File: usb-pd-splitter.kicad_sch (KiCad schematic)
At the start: 5 parts, among them J1 USB_C_Receptacle_USB2.0_14P, J2 USB_C_Receptacle_USB2.0_14P, J3 USB_C_Receptacle_USB2.0_14P

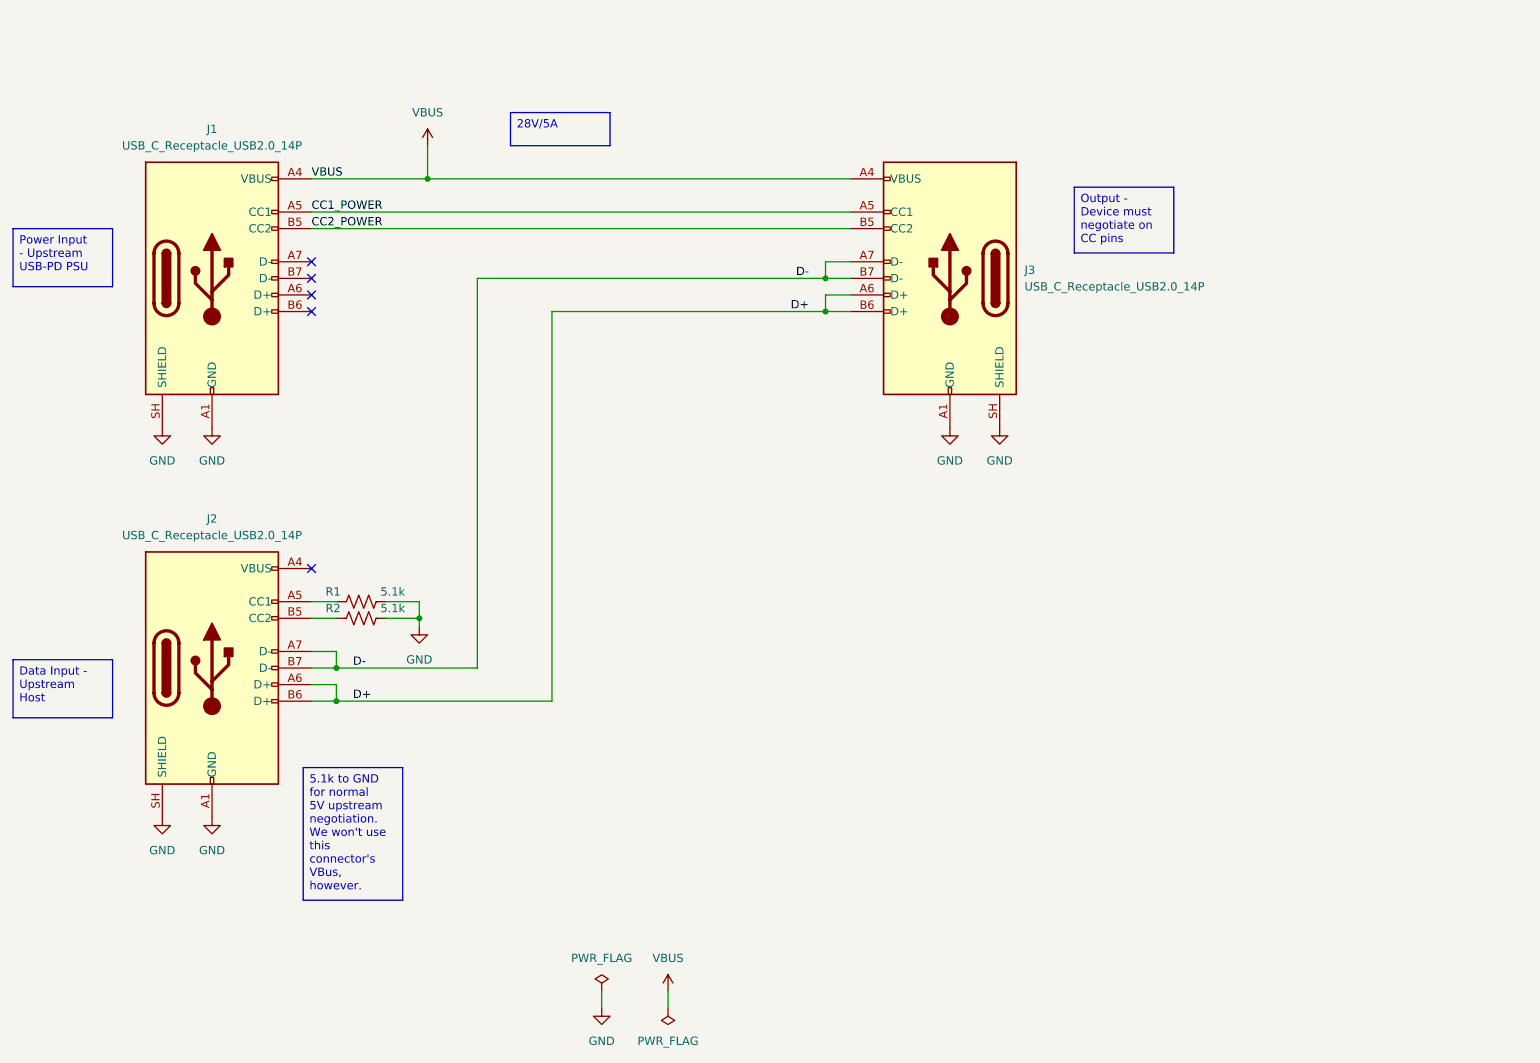
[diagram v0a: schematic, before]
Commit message: routing complete, drc pass
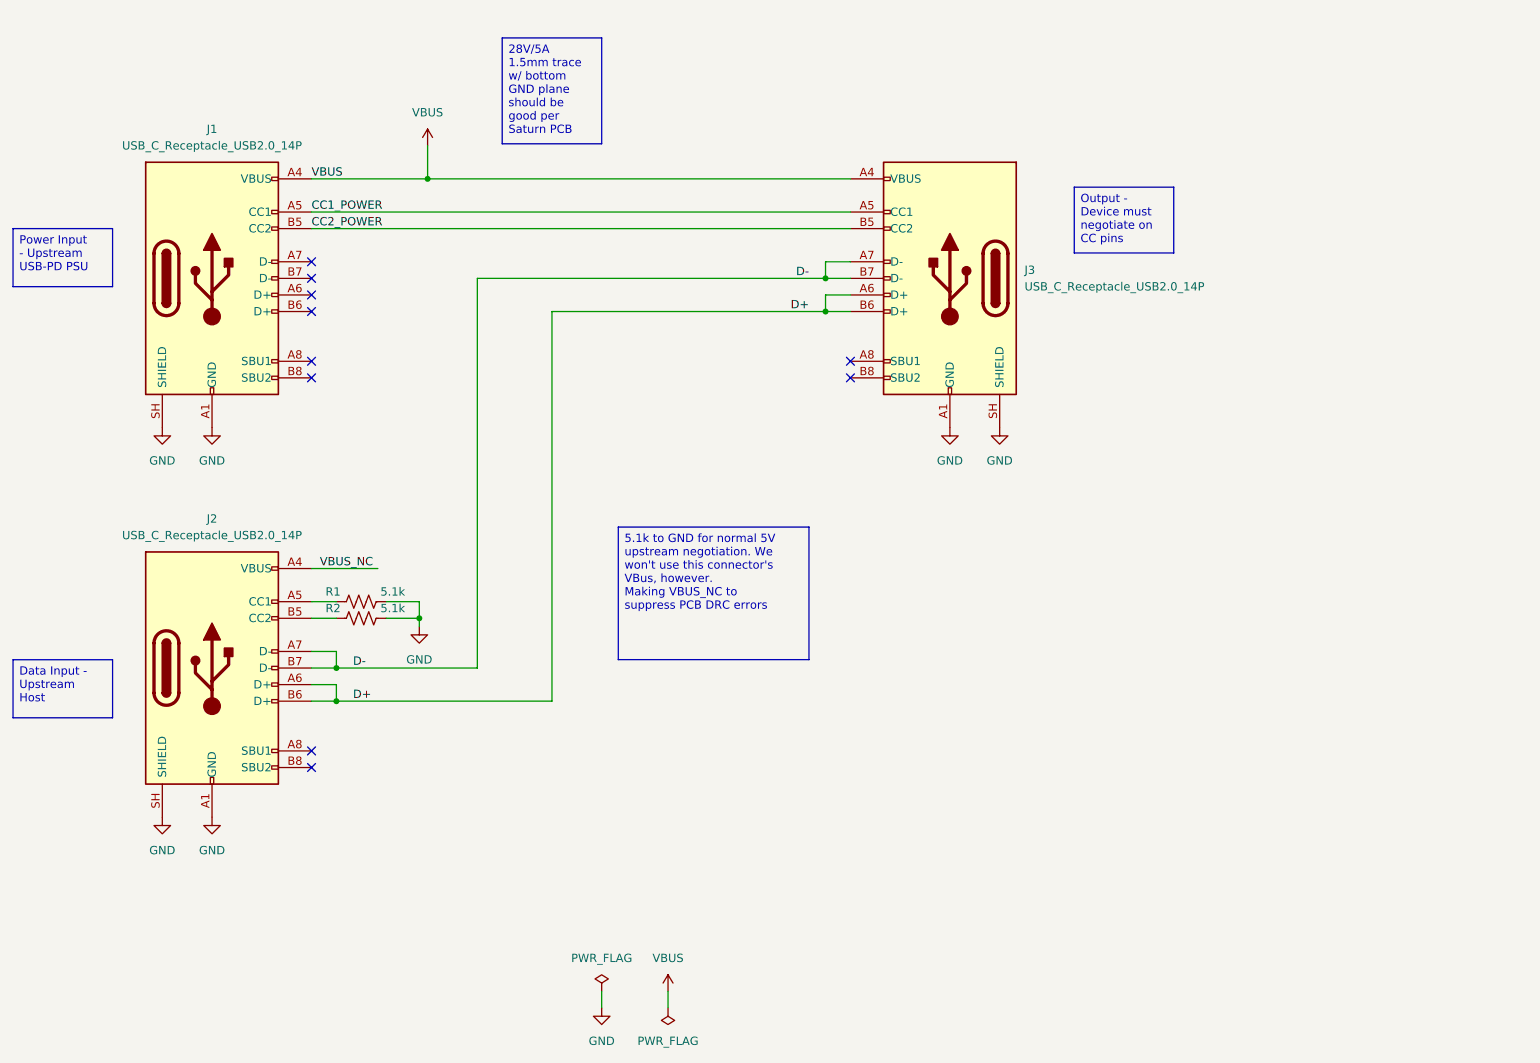
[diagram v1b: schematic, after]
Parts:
- J1, J2, J3: symbol Connector:USB_C_Receptacle_USB2.0_14P -> Connector:USB_C_Receptacle_USB2.0_16P
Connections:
- net VBUS_NC: now reaches J2.A4 (VBUS), J2.A9 (VBUS), J2.B4 (VBUS), J2.B9 (VBUS)
- no-connect marks 5 -> 10
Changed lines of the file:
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@@
 		)
 	)
-	(text_box "28V/5A\n"
+	(text_box "28V/5A\n1.5mm trace w/ bottom GND plane should be good per Saturn PCB"
 		(exclude_from_sim no)
-		(at 107.95 45.72 0)
-		(size 15.24 5.08)
+		(at 106.68 34.29 0)
+		(size 15.24 16.2161)
 		(margins 0.9525 0.9525 0.9525 0.9525)
 		(stroke
@@
 		)
 	)
-	(text_box "5.1k to GND for normal 5V upstream negotiation. We won't use this connector's VBus, however.\n"
+	(text_box "5.1k to GND for normal 5V upstream negotiation. We won't use this connector's VBus, however.\nMaking VBUS_NC to suppress PCB DRC errors\n"
 		(exclude_from_sim no)
-		(at 76.2 146.0647 0)
-		(size 15.24 20.3053)
+		(at 124.46 109.22 0)
+		(size 29.21 20.3053)
 		(margins 0.9525 0.9525 0.9525 0.9525)
 		(stroke
@@
 	)
 	(no_connect
+		(at 160.02 86.36)
+	)
+	(no_connect
+		(at 77.47 86.36)
+	)
+	(no_connect
+		(at 77.47 143.51)
+	)
+	(no_connect
+		(at 77.47 83.82)
+	)
+	(no_connect
+		(at 160.02 83.82)
+	)
+	(no_connect
+		(at 77.47 146.05)
+	)
+	(no_connect
 		(at 77.47 73.66)
 	)
@@
 		(at 77.47 76.2)
 	)
-	(no_connect
-		(at 77.47 115.57)
-	)
 	(wire
 		(pts
@@
 		(pts
 			(xy 160.02 71.12) (xy 156.21 71.12)
+		)
+		(stroke
+			(width 0)
+			(type default)
+		)
+	)
+	(wire
+		(pts
+			(xy 77.47 115.57) (xy 87.63 115.57)
 		)
 		(stroke
@@
 	(label "VBUS"
 		(at 77.47 55.88 0)
+		(effects
+			(font
+				(size 1.27 1.27)
+			)
+			(justify left bottom)
+		)
+	)
+	(label "VBUS_NC"
+		(at 78.74 115.57 0)
 		(effects
 			(font
@@
 	)
 	(symbol
-		(lib_id "Connector:USB_C_Receptacle_USB2.0_14P")
+		(lib_id "Connector:USB_C_Receptacle_USB2.0_16P")
 		(at 62.23 130.81 0)
 		(unit 1)
@@
 		)
 		(pin "B1"
+		)
+		(pin "B8"
+		)
+		(pin "A8"
 		)
 		(instances
@@
 	)
 	(symbol
-		(lib_id "Connector:USB_C_Receptacle_USB2.0_14P")
+		(lib_id "Connector:USB_C_Receptacle_USB2.0_16P")
 		(at 175.26 71.12 0)
 		(mirror y)
@@
 		)
 		(pin "A9"
+		)
+		(pin "B8"
+		)
+		(pin "A8"
 		)
 		(instances
@@
 	)
 	(symbol
-		(lib_id "Connector:USB_C_Receptacle_USB2.0_14P")
+		(lib_id "Connector:USB_C_Receptacle_USB2.0_16P")
 		(at 62.23 71.12 0)
 		(unit 1)
@@
 		(pin "B7"
 		)
+		(pin "A8"
+		)
+		(pin "B8"
+		)
 		(instances

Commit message: Add deterministic hardware release workflow and README 3D render
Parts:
- J1, J2, J3: BOM Comments (none) -> JLCPCB extended part; high assembly difficulty; fixture req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; LCSC Part # (none) -> C5143397; MPN (none) -> USB4110-GF-A; Manufacturer (none) -> Global Connector Technology
- R1, R2: BOM Comments (none) -> JLCPCB basic part; 5.1 kOhm 1% 125 mW; LCSC Part # (none) -> C27834; MPN (none) -> 0805W8F5101T5E; Manufacturer (none) -> UNI-ROYAL
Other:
- title: (none) -> USB-PD Splitter
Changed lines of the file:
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@@
 	(generator_version "10.0")
 	(paper "A4")
+	(title_block
+		(title "USB-PD Splitter")
+		(date "2026-07-18")
+		(rev "A")
+		(comment 1 "Professional fabrication and assembly release")
+		(comment 2 "Hardware version 1.0.0")
+	)
 	(text_box "Output - Device must negotiate on CC pins"
 		(exclude_from_sim no)
@@
 	(wire
 		(pts
-			(xy 77.47 115.57) (xy 87.63 115.57)
+			(xy 77.47 115.57) (xy 78.74 115.57)
 		)
 		(stroke
@@
 			)
 		)
-		(property "Datasheet" "https://www.usb.org/sites/default/files/documents/usb_type-c.zip"
+		(property "Datasheet" "https://gct.co/files/drawings/usb4110.pdf"
 			(at 66.04 130.81 0)
 			(hide yes)
@@
 			)
 		)
+		(property "Manufacturer" "Global Connector Technology" (at 62.23 130.81 0) (hide yes) (effects (font (size 1.27 1.27))))
+		(property "MPN" "USB4110-GF-A" (at 62.23 130.81 0) (hide yes) (effects (font (size 1.27 1.27))))
+		(property "LCSC Part #" "C5143397" (at 62.23 130.81 0) (hide yes) (effects (font (size 1.27 1.27))))
+		(property "BOM Comments" "JLCPCB extended part; high assembly difficulty; fixture required" (at 62.23 130.81 0) (hide yes) (effects (font (size 1.27 1.27))))
 		(pin "A4"
 		)
@@
 			)
 		)
-		(property "Datasheet" ""
+		(property "Datasheet" "https://www.lcsc.com/product-detail/C27834.html"
 			(at 85.09 120.65 0)
 			(hide yes)
@@
 			)
 		)
+		(property "Manufacturer" "UNI-ROYAL" (at 85.09 120.65 0) (hide yes) (effects (font (size 1.27 1.27))))
+		(property "MPN" "0805W8F5101T5E" (at 85.09 120.65 0) (hide yes) (effects (font (size 1.27 1.27))))
+		(property "LCSC Part #" "C27834" (at 85.09 120.65 0) (hide yes) (effects (font (size 1.27 1.27))))
+		(property "BOM Comments" "JLCPCB basic part; 5.1 kOhm 1% 125 mW" (at 85.09 120.65 0) (hide yes) (effects (font (size 1.27 1.27))))
 		(pin "2"
 		)
@@
 			)
 		)
-		(property "Datasheet" "https://www.usb.org/sites/default/files/documents/usb_type-c.zip"
+		(property "Datasheet" "https://gct.co/files/drawings/usb4110.pdf"
 			(at 171.45 71.12 0)
 			(hide yes)
@@
 			)
 		)
+		(property "Manufacturer" "Global Connector Technology" (at 175.26 71.12 0) (hide yes) (effects (font (size 1.27 1.27))))
+		(property "MPN" "USB4110-GF-A" (at 175.26 71.12 0) (hide yes) (effects (font (size 1.27 1.27))))
+		(property "LCSC Part #" "C5143397" (at 175.26 71.12 0) (hide yes) (effects (font (size 1.27 1.27))))
+		(property "BOM Comments" "JLCPCB extended part; high assembly difficulty; fixture required" (at 175.26 71.12 0) (hide yes) (effects (font (size 1.27 1.27))))
 		(pin "B5"
 		)
@@
 			)
 		)
-		(property "Datasheet" ""
+		(property "Datasheet" "https://www.lcsc.com/product-detail/C27834.html"
 			(at 85.09 123.19 0)
 			(hide yes)
@@
 			)
 		)
+		(property "Manufacturer" "UNI-ROYAL" (at 85.09 123.19 0) (hide yes) (effects (font (size 1.27 1.27))))
+		(property "MPN" "0805W8F5101T5E" (at 85.09 123.19 0) (hide yes) (effects (font (size 1.27 1.27))))
+		(property "LCSC Part #" "C27834" (at 85.09 123.19 0) (hide yes) (effects (font (size 1.27 1.27))))
+		(property "BOM Comments" "JLCPCB basic part; 5.1 kOhm 1% 125 mW" (at 85.09 123.19 0) (hide yes) (effects (font (size 1.27 1.27))))
 		(pin "2"
 		)
@@
 			)
 		)
-		(property "Datasheet" "https://www.usb.org/sites/default/files/documents/usb_type-c.zip"
+		(property "Datasheet" "https://gct.co/files/drawings/usb4110.pdf"
 			(at 66.04 71.12 0)
 			(hide yes)
@@
 			)
 		)
+		(property "Manufacturer" "Global Connector Technology" (at 62.23 71.12 0) (hide yes) (effects (font (size 1.27 1.27))))
+		(property "MPN" "USB4110-GF-A" (at 62.23 71.12 0) (hide yes) (effects (font (size 1.27 1.27))))
+		(property "LCSC Part #" "C5143397" (at 62.23 71.12 0) (hide yes) (effects (font (size 1.27 1.27))))
+		(property "BOM Comments" "JLCPCB extended part; high assembly difficulty; fixture required" (at 62.23 71.12 0) (hide yes) (effects (font (size 1.27 1.27))))
 		(pin "B6"
 		)

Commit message: release: prepare hardware v1.1.0
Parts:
- added D1: Green, LED_SMD:LED_0805_2012Metric, symbol Device:LED
- added R3: 10k, Resistor_SMD:R_0805_2012Metric_Pad1.20x1.40mm_HandSolder, symbol Device:R_US
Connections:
- net GND: now also R3.2
- net VBUS: now also D1.2 (A)
- new net: D1.1 (K), R3.1
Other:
- note added: "Green LED to indicate power on"
- note added: "Power Indicator"
